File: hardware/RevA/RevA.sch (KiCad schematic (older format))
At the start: 143 parts, among them J1 USB_C_Receptacle_USB2.0, J2 DNP Conn_02x02_Odd_Even, J3 DNP Conn_01x02, J4 DNP Conn_02x03_Odd_Even, J5 DNP Conn_01x02, SW1 SW_Push, SW2 SW_Push, U1 SY8120B1ABC, U10 SPI RAM LY68L6400SLIT, U2 XC6206P25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

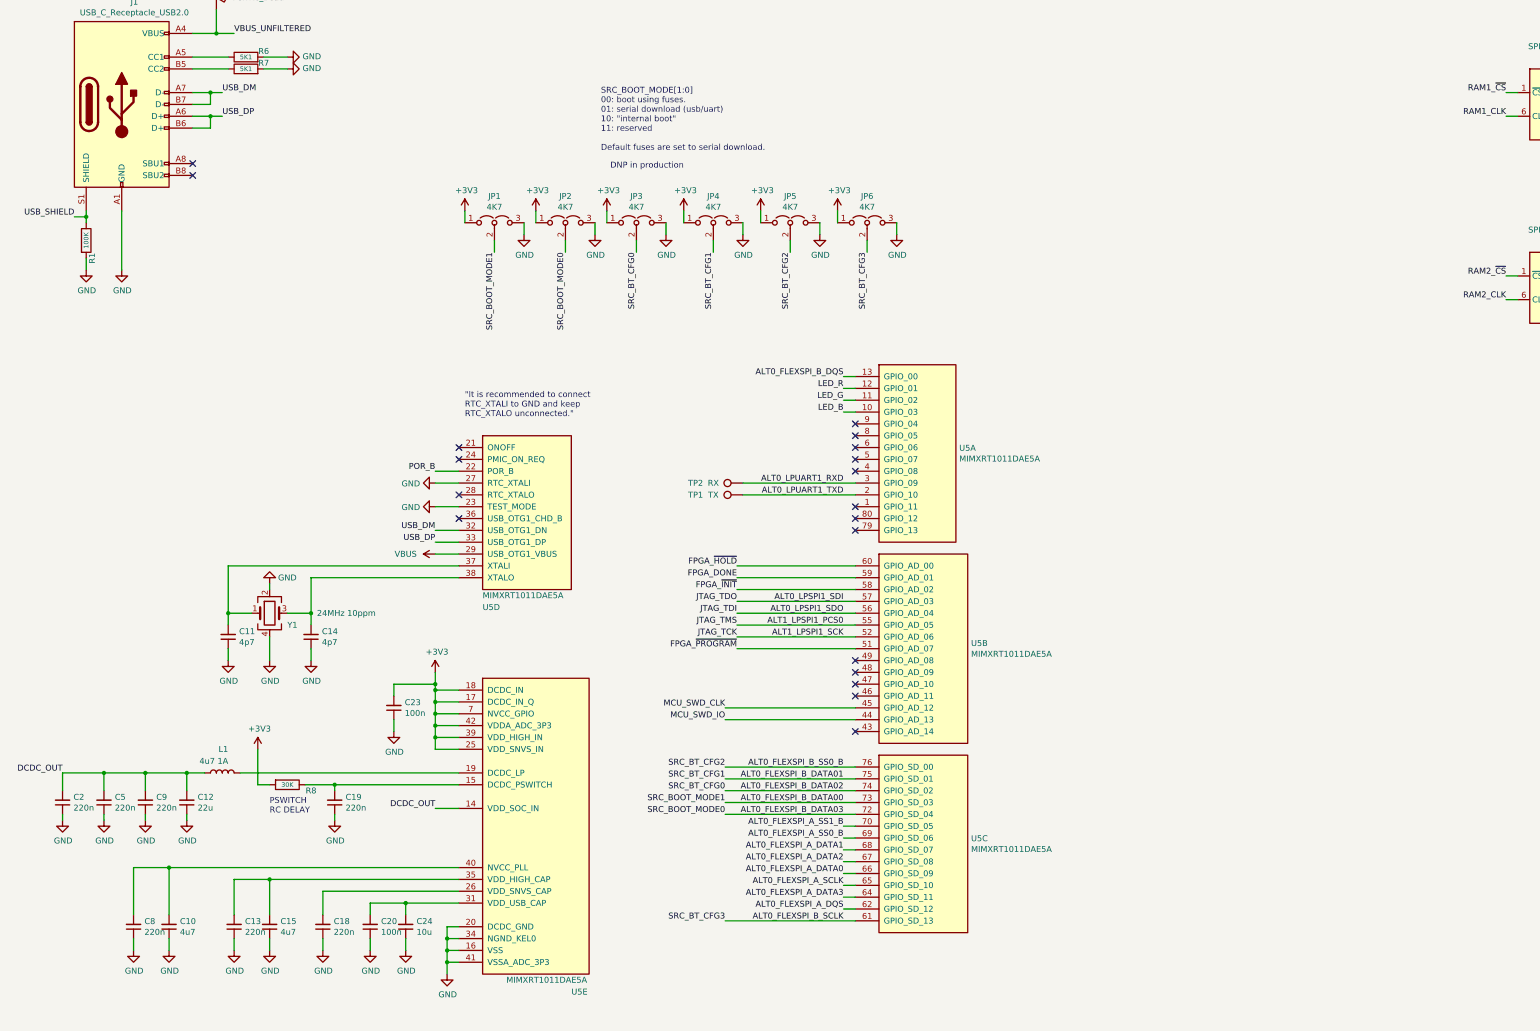
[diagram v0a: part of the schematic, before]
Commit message: Add errata/todo
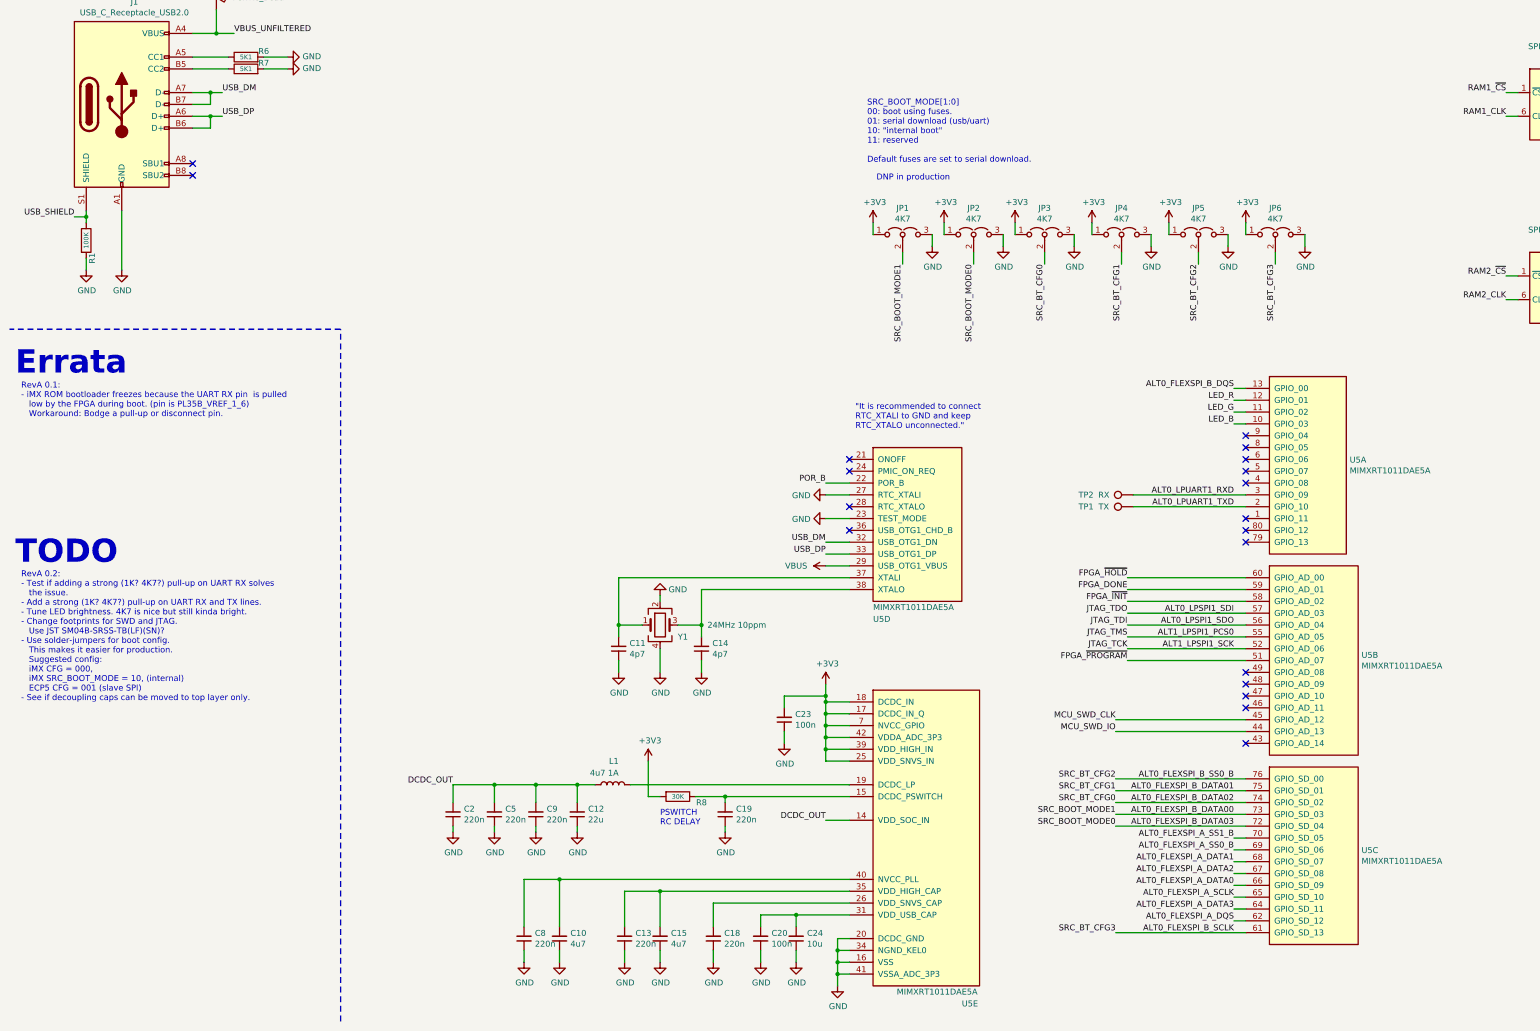
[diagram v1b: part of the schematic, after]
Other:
- note added: "Errata"
- note added: "RevA 0.1:\n- iMX ROM bootloader freezes because the UART RX pin is pulled\n low by the FPGA during boot. (pin is PL35B_VREF_1_6)\n Workaround: Bodge a pull-up or disconnect pin."
- note added: "RevA 0.2:\n- Test if adding a strong (1K? 4K7?) pull-up on UART RX solves\n the issue.\n- Add a strong (1K? 4K7?) pull-up on UART RX and TX lines.\n- Tune LED brightness. 4K7 is nice but still kinda bright.\n- Change footprints for SWD and JTAG.\n Use JST SM04B-SRSS-TB(LF)(SN)?\n- Use solder-jumpers for boot config.\n This makes it easier for production.\n Suggested config:\n iMX CFG = 000,\n iMX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"
- note added: "TODO"
- moved on the sheet: C10, C11, C12, C13, C14, C15, C18, C19, C2, C20, C23, C24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

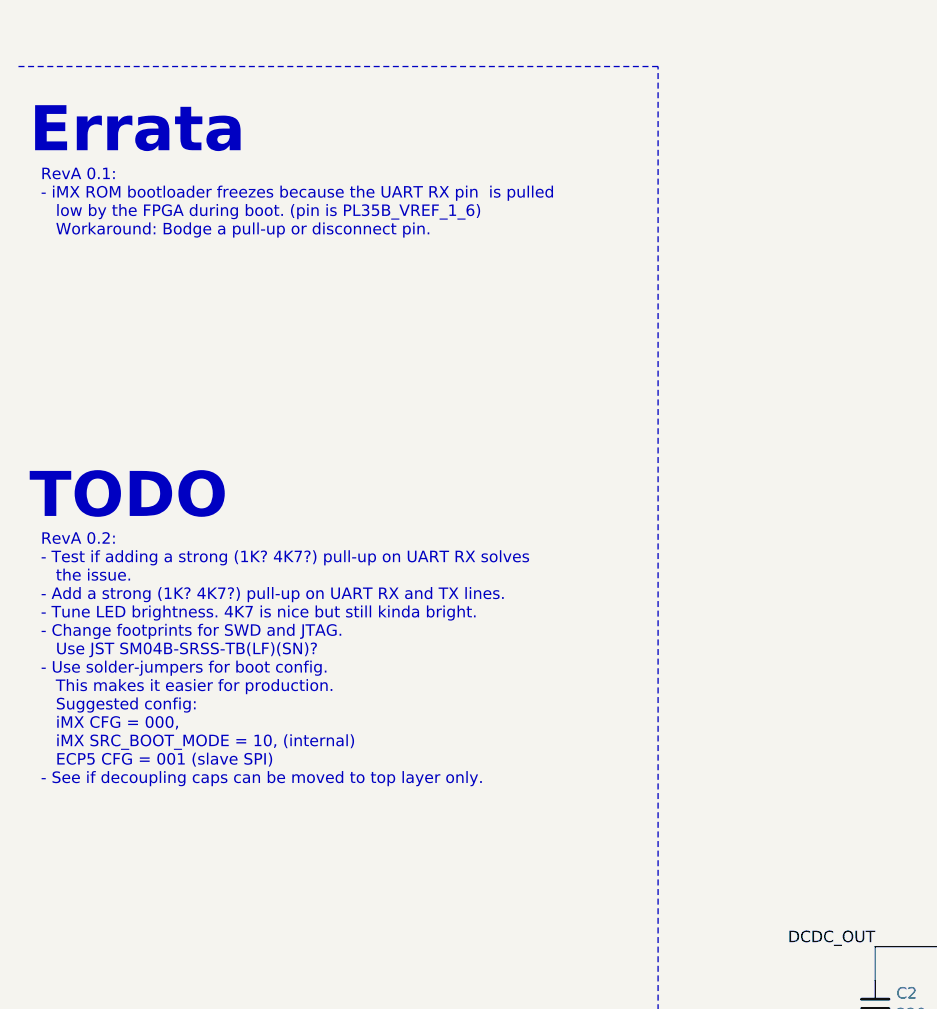
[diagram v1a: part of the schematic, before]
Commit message: Update errata/todo
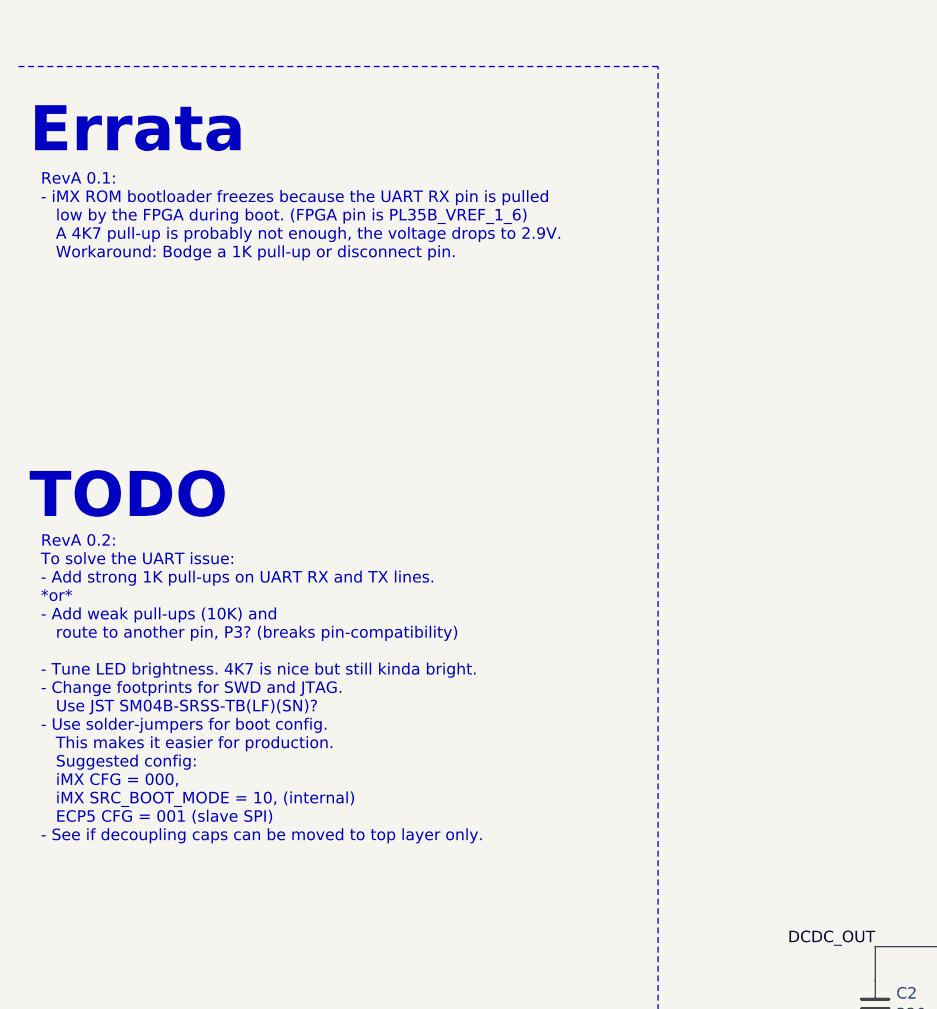
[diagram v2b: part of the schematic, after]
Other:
- note added: "RevA 0.1:\n- iMX ROM bootloader freezes because the UART RX pin is pulled\n low by the FPGA during boot. (FPGA pin is PL35B_VREF_1_6)\n A 4K7 pull-up is probably not enough, the voltage drops to 2.9V.\n Workaround: Bodge a 1K pull-up or disconnect pin.\n"
- note added: "RevA 0.2:\nTo solve the UART issue:\n- Add strong 1K pull-ups on UART RX and TX lines.\n*or*\n- Add weak pull-ups (10K) and\n route to another pin, P3? (breaks pin-compatibility)\n\n- Tune LED brightness. 4K7 is nice but still kinda bright.\n- Change footprints for SWD and JTAG.\n Use JST SM04B-SRSS-TB(LF)(SN)?\n- Use solder-jumpers for boot config.\n This makes it easier for production.\n Sugges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"
- note removed: "RevA 0.1:\n- iMX ROM bootloader freezes because the UART RX pin is pulled\n low by the FPGA during boot. (pin is PL35B_VREF_1_6)\n Workaround: Bodge a pull-up or disconnect pin."
- note removed: "RevA 0.2:\n- Test if adding a strong (1K? 4K7?) pull-up on UART RX solves\n the issue.\n- Add a strong (1K? 4K7?) pull-up on UART RX and TX lines.\n- Tune LED brightness. 4K7 is nice but still kinda bright.\n- Change footprints for SWD and JTAG.\n Use JST SM04B-SRSS-TB(LF)(SN)?\n- Use solder-jumpers for boot config.\n This makes it easier for production.\n Suggested config:\n iMX CFG = 000,\n iMX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"
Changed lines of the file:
@@
 Text Notes 600  10600 0    197  ~ 39
 Errata
-Text Notes 650  10950 0    50   ~ 0
-RevA 0.1:\n- iMX ROM bootloader freezes because the UART RX pin  is pulled\n   low by the FPGA during boot. (pin is PL35B_VREF_1_6)\n   Workaround: Bodge a pull-up or disconnect pin.
+Text Notes 650  11050 0    50   ~ 0
+RevA 0.1:\n- iMX ROM bootloader freezes because the UART RX pin is pulled\n   low by the FPGA during boot. (FPGA pin is PL35B_VREF_1_6)\n   A 4K7 pull-up is probably not enough, the voltage drops to 2.9V.\n   Workaround: Bodge a 1K pull-up or disconnect pin.\n
 Text Notes 600  12200 0    197  ~ 39
 TODO
-Text Notes 650  13350 0    50   ~ 0
-RevA 0.2:\n- Test if adding a strong (1K? 4K7?) pull-up on UART RX solves\n   the issue.\n- Add a strong (1K? 4K7?) pull-up on UART RX and TX lines.\n- Tune LED brightness. 4K7 is nice but still kinda bright.\n- Change footprints for SWD and JTAG.\n   Use JST SM04B-SRSS-TB(LF)(SN)?\n- Use solder-jumpers for boot config.\n   This makes it easier for production.\n   Suggested config:\n   iMX CFG = 000,\n   iMX SRC_BOOT_MODE = 10, (internal)\n   ECP5 CFG = 001 (slave SPI)\n- See if decoupling caps can be moved to top layer only.
+Text Notes 650  13600 0    50   ~ 0
+RevA 0.2:\nTo solve the UART issue:\n- Add strong 1K pull-ups on UART RX and TX lines.\n*or*\n- Add weak pull-ups (10K) and\n   route to another pin, P3? (breaks pin-compatibility)\n\n- Tune LED brightness. 4K7 is nice but still kinda bright.\n- Change footprints for SWD and JTAG.\n   Use JST SM04B-SRSS-TB(LF)(SN)?\n- Use solder-jumpers for boot config.\n   This makes it easier for production.\n   Suggested config:\n   iMX CFG = 000,\n   iMX SRC_BOOT_MODE = 10, (internal)\n   ECP5 CFG = 001 (slave SPI)\n- See if decoupling caps can be moved to top layer only.
 $EndSCHEMATC
